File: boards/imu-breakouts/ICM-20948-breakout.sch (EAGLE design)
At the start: 7 parts, among them U1 ICM-20948, U3 ICM-42605

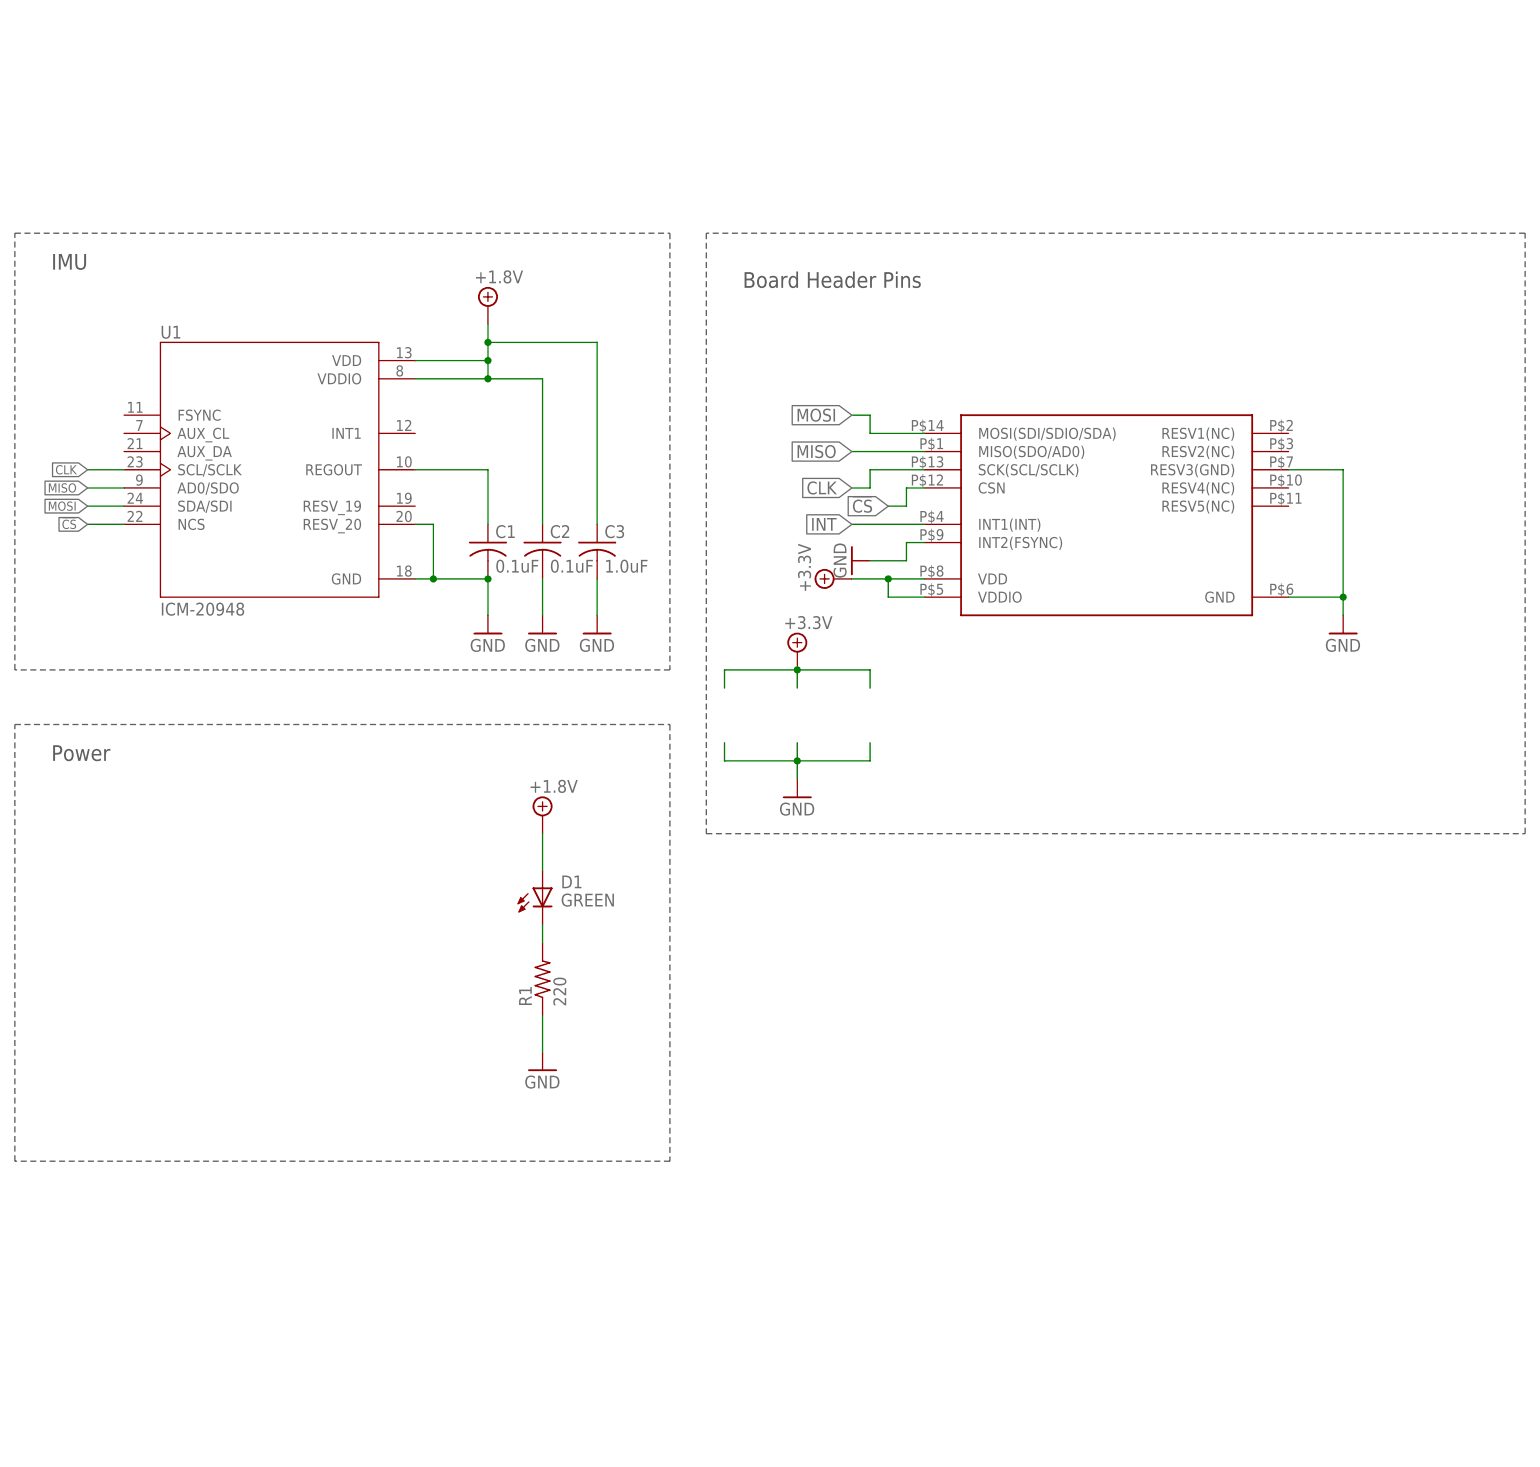
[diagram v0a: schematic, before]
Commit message: updated icm20948 breakout
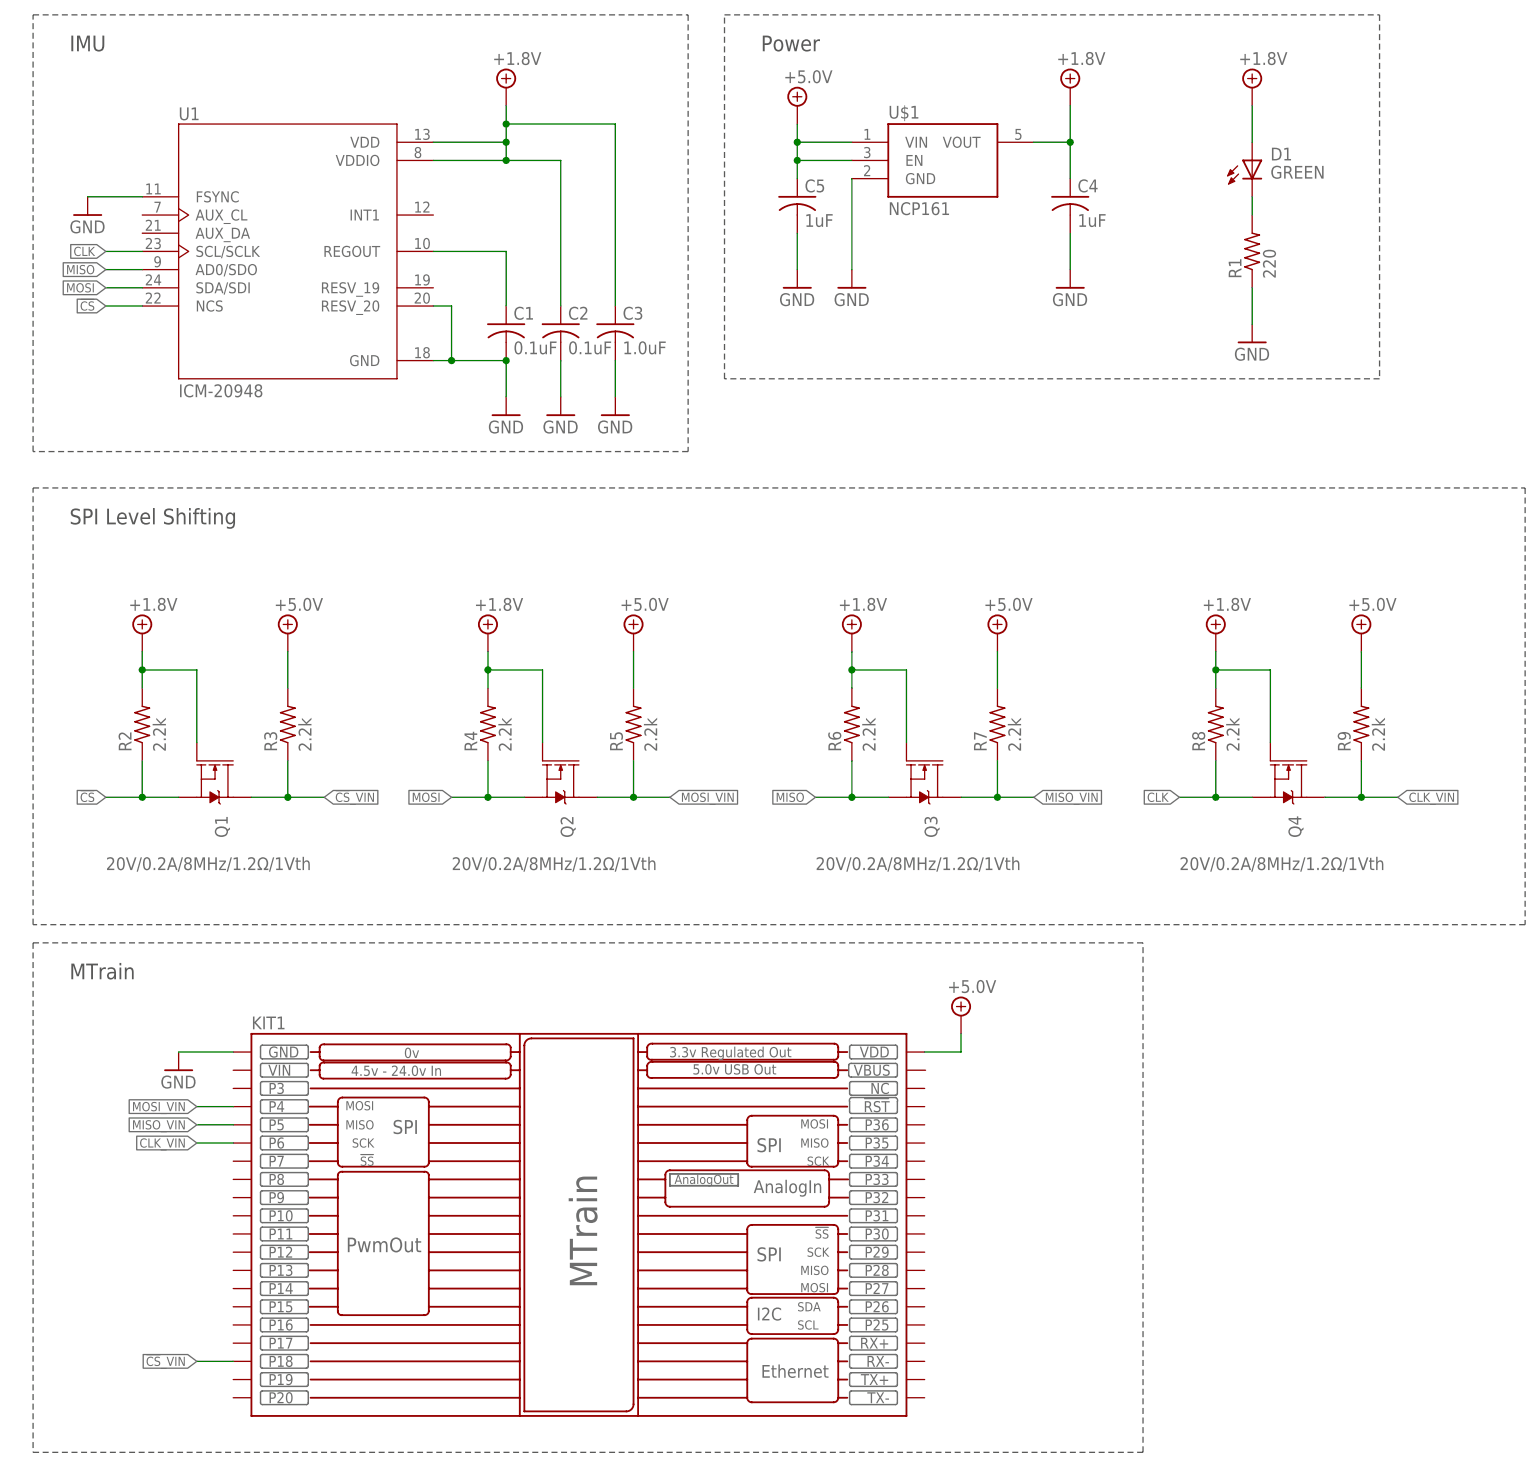
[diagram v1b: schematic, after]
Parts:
- removed U3: ICM-42605, RoboJackets-Sensors:ICM-42605
- added C4, C5: 1uF, rcl:C-USC0603
- added KIT1: MTRAIN, RoboJackets-Boards:MTRAIN
- added Q1, Q2, Q3, Q4: 20V/0.2A/8MHz/1.2Ω/1Vth, SparkFun-DiscreteSemi:MOSFET-NCH-RE1C002UN
- added R2, R3, R4, R5, R6, R7, R8, R9: 2.2k, RoboJackets-Resistors:R0603W
- added U$1: NCP161, RoboJackets-PowerICs:NCP161
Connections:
- net N$2 renamed REGOUT
- removed net INT: U3.INT1(INT)
- new net !CS!_VIN: KIT1.P18, Q1.D, R3.PIN1
- new net +5.0V: KIT1.VDD
- new net CLK_VIN: KIT1.P6, Q4.D, R9.PIN1
- new net MISO_VIN: KIT1.P5, Q3.D, R7.PIN1
- new net MOSI_VIN: KIT1.P4, Q2.D, R5.PIN1
- net !CS!: now also Q1.S, Q2.S, R2.PIN1, R4.PIN1; no longer U3.CSN
- net +1.8V: now also C4.1, Q1.G, Q2.G, Q3.G, Q4.G, R2.PIN2, R4.PIN2, R6.PIN2, R8.PIN2, U$1.VOUT
- net +3.3V: now also C5.1, R3.PIN2, R5.PIN2, R7.PIN2, R9.PIN2, U$1.EN, U$1.VIN; no longer U3.VDD, U3.VDDIO
- net CLK: now also Q4.S, R8.PIN1; no longer U3.SCK(SCL/SCLK)
- net GND: now also C4.2, C5.2, KIT1.GND, U$1.GND, U1.FSYNC; no longer U3.GND, U3.INT2(FSYNC), U3.RESV3(GND)
- net MISO: now also Q3.S, R6.PIN1; no longer U3.MISO(SDO/AD0)
- net MOSI: no longer U3.MOSI(SDI/SDIO/SDA)
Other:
- note added: "MTrain"
- note added: "SPI Level Shifting"
- note removed: "Board Header Pins"
- moved on the sheet: C1, C2, C3, D1, R1, U1

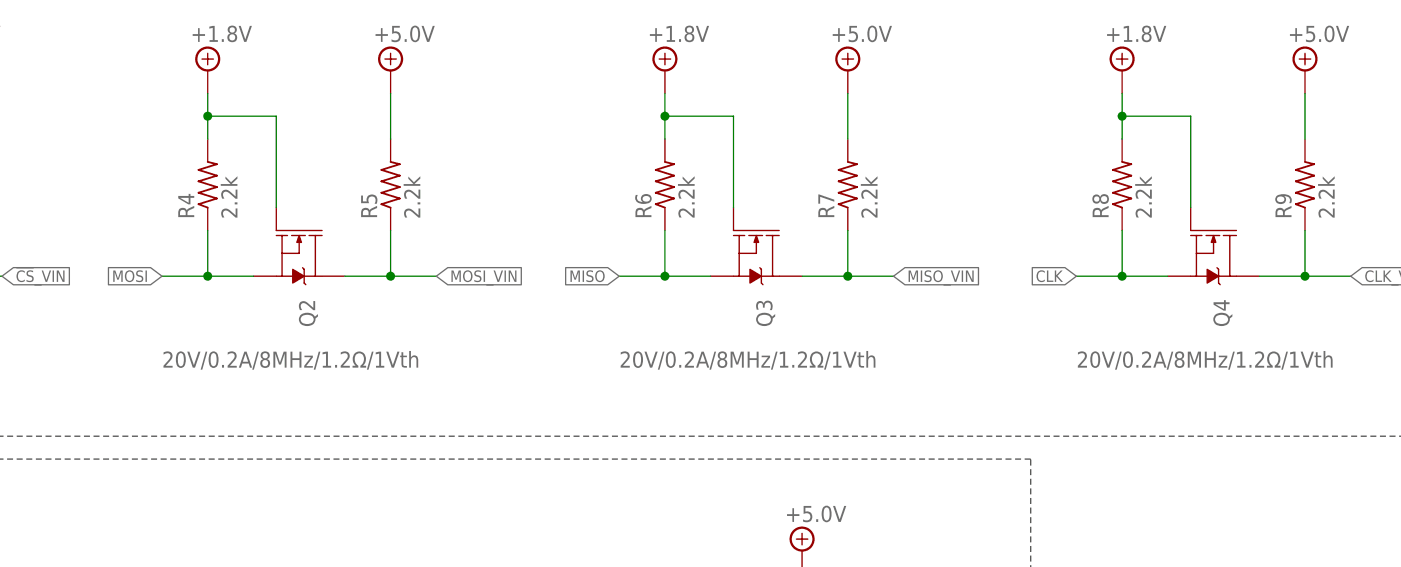
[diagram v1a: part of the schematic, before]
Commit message: added ICM 20948 breakout
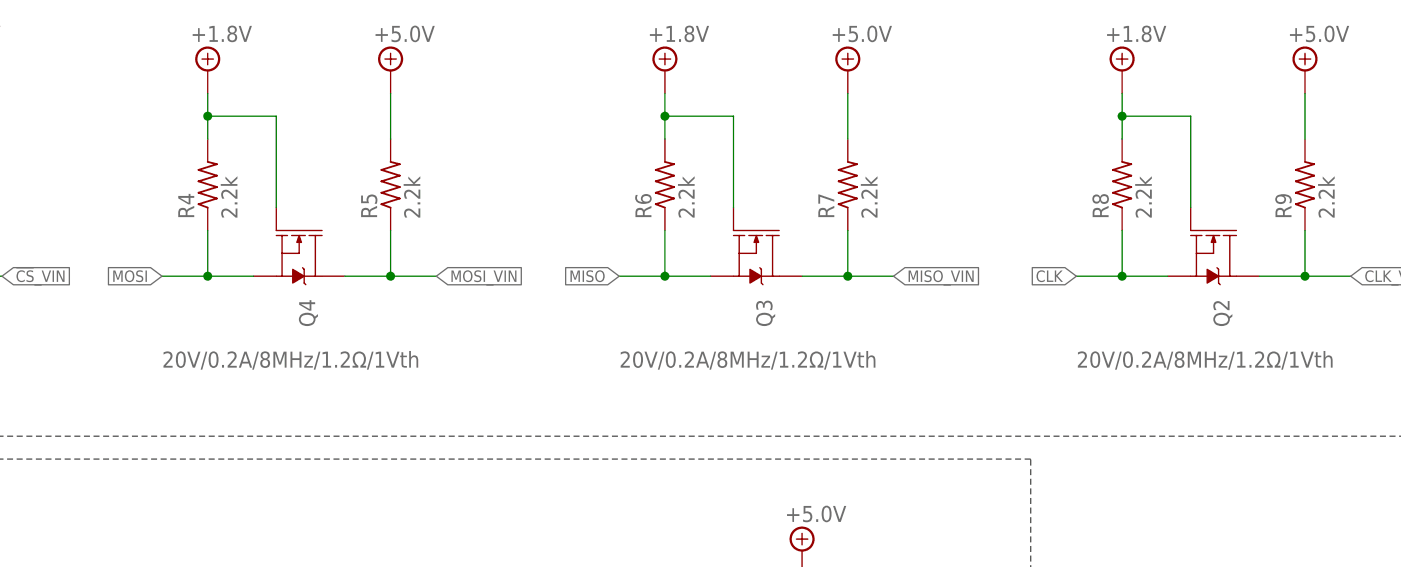
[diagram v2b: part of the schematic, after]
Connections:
- net !CS!: no longer Q2.S, R4.PIN1
- net CLK: now also Q2.S; no longer Q4.S
- net CLK_VIN: now also Q2.D; no longer Q4.D
- net MOSI: now also Q4.S, R4.PIN1
- net MOSI_VIN: now also Q4.D; no longer Q2.D
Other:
- moved on the sheet: Q2, Q4
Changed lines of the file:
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@@
 <part name="R3" library="RoboJackets-Resistors" deviceset="R0603W" device="" value="2.2k"/>
 <part name="SUPPLY5" library="RoboJackets-Supplies" deviceset="+5.0V" device=""/>
-<part name="Q2" library="SparkFun-DiscreteSemi" deviceset="MOSFET-NCH" device="-RE1C002UN" value="20V/0.2A/8MHz/1.2Ω/1Vth"/>
+<part name="Q4" library="SparkFun-DiscreteSemi" deviceset="MOSFET-NCH" device="-RE1C002UN" value="20V/0.2A/8MHz/1.2Ω/1Vth"/>
 <part name="R4" library="RoboJackets-Resistors" deviceset="R0603W" device="" value="2.2k"/>
 <part name="SUPPLY7" library="RoboJackets-Supplies" deviceset="+1.8V" device=""/>
@@
 <part name="R7" library="RoboJackets-Resistors" deviceset="R0603W" device="" value="2.2k"/>
 <part name="SUPPLY10" library="RoboJackets-Supplies" deviceset="+5.0V" device=""/>
-<part name="Q4" library="SparkFun-DiscreteSemi" deviceset="MOSFET-NCH" device="-RE1C002UN" value="20V/0.2A/8MHz/1.2Ω/1Vth"/>
+<part name="Q2" library="SparkFun-DiscreteSemi" deviceset="MOSFET-NCH" device="-RE1C002UN" value="20V/0.2A/8MHz/1.2Ω/1Vth"/>
 <part name="R8" library="RoboJackets-Resistors" deviceset="R0603W" device="" value="2.2k"/>
 <part name="SUPPLY11" library="RoboJackets-Supplies" deviceset="+1.8V" device=""/>
@@
 <attribute name="VALUE" x="43.815" y="122.555" size="1.778" layer="96"/>
 </instance>
-<instance part="Q2" gate="NMOS" x="83.82" y="99.06" smashed="yes" rot="R270">
+<instance part="Q4" gate="NMOS" x="83.82" y="99.06" smashed="yes" rot="R270">
 <attribute name="NAME" x="83.82" y="93.98" size="1.778" layer="95" font="vector" rot="R270"/>
 <attribute name="VALUE" x="68.58" y="86.36" size="1.778" layer="96" font="vector"/>
@@
 <attribute name="VALUE" x="142.875" y="122.555" size="1.778" layer="96"/>
 </instance>
-<instance part="Q4" gate="NMOS" x="185.42" y="99.06" smashed="yes" rot="R270">
+<instance part="Q2" gate="NMOS" x="185.42" y="99.06" smashed="yes" rot="R270">
 <attribute name="NAME" x="185.42" y="93.98" size="1.778" layer="95" font="vector" rot="R270"/>
 <attribute name="VALUE" x="170.18" y="86.36" size="1.778" layer="96" font="vector"/>
@@
 </segment>
 <segment>
+<pinref part="Q4" gate="NMOS" pin="S"/>
+<pinref part="R4" gate="G$1" pin="PIN1"/>
+<wire x1="78.74" y1="96.52" x2="73.66" y2="96.52" width="0.1524" layer="91"/>
+<wire x1="73.66" y1="96.52" x2="73.66" y2="101.6" width="0.1524" layer="91"/>
+<wire x1="73.66" y1="96.52" x2="68.58" y2="96.52" width="0.1524" layer="91"/>
+<junction x="73.66" y="96.52"/>
 <label x="68.58" y="96.52" size="1.27" layer="95" rot="R180" xref="yes"/>
 </segment>
@@
 <segment>
 <pinref part="R8" gate="G$1" pin="PIN1"/>
-<pinref part="Q4" gate="NMOS" pin="S"/>
+<pinref part="Q2" gate="NMOS" pin="S"/>
 <wire x1="175.26" y1="101.6" x2="175.26" y2="96.52" width="0.1524" layer="91"/>
 <wire x1="175.26" y1="96.52" x2="180.34" y2="96.52" width="0.1524" layer="91"/>
@@
 <junction x="25.4" y="96.52"/>
 <label x="20.32" y="96.52" size="1.27" layer="95" rot="R180" xref="yes"/>
-</segment>
-<segment>
-<pinref part="R4" gate="G$1" pin="PIN1"/>
-<pinref part="Q2" gate="NMOS" pin="S"/>
-<wire x1="73.66" y1="101.6" x2="73.66" y2="96.52" width="0.1524" layer="91"/>
-<wire x1="73.66" y1="96.52" x2="78.74" y2="96.52" width="0.1524" layer="91"/>
-<wire x1="68.58" y1="96.52" x2="73.66" y2="96.52" width="0.1524" layer="91"/>
-<junction x="73.66" y="96.52"/>
 </segment>
 </net>
@@
 <pinref part="R4" gate="G$1" pin="PIN2"/>
 <wire x1="73.66" y1="116.84" x2="73.66" y2="114.3" width="0.1524" layer="91"/>
-<pinref part="Q2" gate="NMOS" pin="G"/>
+<pinref part="Q4" gate="NMOS" pin="G"/>
 <wire x1="73.66" y1="114.3" x2="73.66" y2="111.76" width="0.1524" layer="91"/>
 <wire x1="81.28" y1="104.14" x2="81.28" y2="114.3" width="0.1524" layer="91"/>
@@
 <pinref part="R8" gate="G$1" pin="PIN2"/>
 <wire x1="175.26" y1="116.84" x2="175.26" y2="114.3" width="0.1524" layer="91"/>
-<pinref part="Q4" gate="NMOS" pin="G"/>
+<pinref part="Q2" gate="NMOS" pin="G"/>
 <wire x1="175.26" y1="114.3" x2="175.26" y2="111.76" width="0.1524" layer="91"/>
 <wire x1="182.88" y1="104.14" x2="182.88" y2="114.3" width="0.1524" layer="91"/>
@@
 <net name="CLK_VIN" class="0">
 <segment>
-<pinref part="Q4" gate="NMOS" pin="D"/>
+<pinref part="Q2" gate="NMOS" pin="D"/>
 <wire x1="190.5" y1="96.52" x2="195.58" y2="96.52" width="0.1524" layer="91"/>
 <pinref part="R9" gate="G$1" pin="PIN1"/>
@@
 </segment>
 <segment>
-<pinref part="Q2" gate="NMOS" pin="D"/>
+<pinref part="Q4" gate="NMOS" pin="D"/>
 <wire x1="88.9" y1="96.52" x2="93.98" y2="96.52" width="0.1524" layer="91"/>
 <pinref part="R5" gate="G$1" pin="PIN1"/>
